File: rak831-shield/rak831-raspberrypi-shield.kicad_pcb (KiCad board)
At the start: 2 copper layers, 59.1 x 73.7 mm, 2 parts, among them P1 CONN_02X20, P2 CONN_02X12

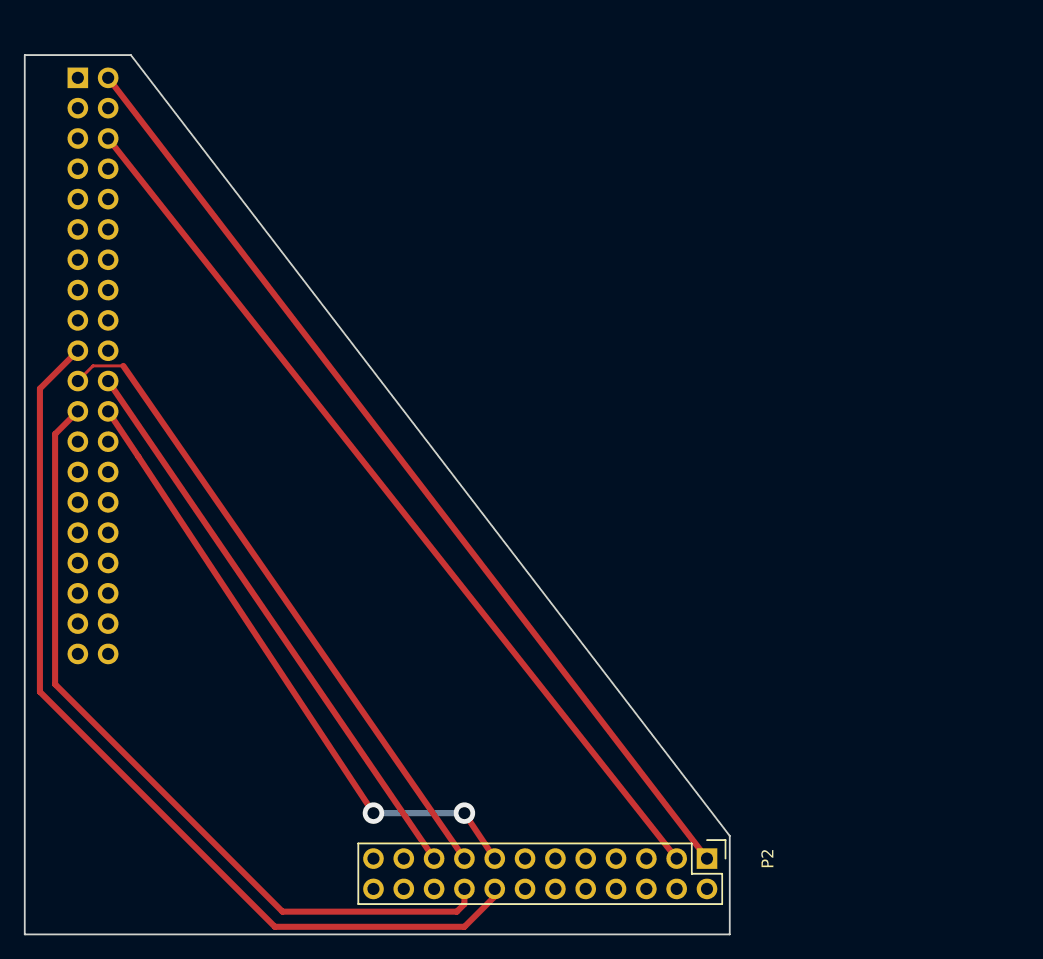
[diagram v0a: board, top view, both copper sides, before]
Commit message: Versión invertida y con pistas más gruesas.
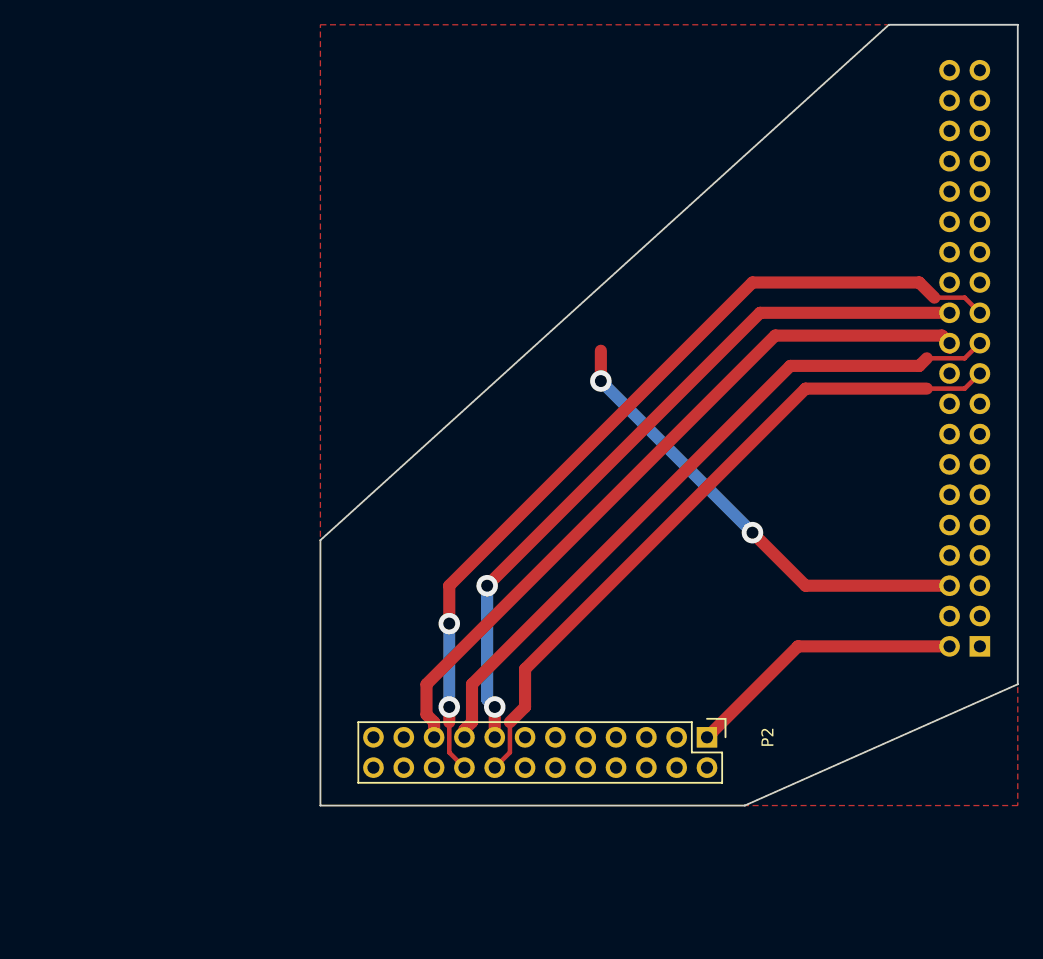
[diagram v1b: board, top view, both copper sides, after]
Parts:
- moved P1 89.3 mm to (134.6, 135.9), turned to 90 degrees
- moved P2 10.2 mm to (111.8, 143.5)
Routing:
- net Net-(P1-Pad2): track 82.4 -> 23.5 mm
- net Net-(P1-Pad6): track 76.9 -> 38.9 mm, vias 0 -> 2
- net Net-(P1-Pad19): track 77.8 -> 57.7 mm
- net Net-(P1-Pad22): track 48.4 -> 61.8 mm
- net Net-(P1-Pad24): track 52.5 -> 61.2 mm
- net Net-(P1-Pad21): track 54.5 -> 59.1 mm
- net Net-(P1-Pad23): track 67.4 -> 71.8 mm, vias 0 -> 2
- added copper zone on F.Cu, net Net-(P1-Pad6)
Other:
- board size 59.1 x 73.7 mm -> 58.4 x 65.4 mm

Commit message: Versión más compacta
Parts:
- moved P2 7.62 mm to (119.4, 143.5)
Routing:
- net Net-(P1-Pad6): track 38.9 -> 51.9 mm
- net Net-(P1-Pad23): track 71.8 -> 61.6 mm, vias 2 -> 0
- net Net-(P1-Pad24): track 61.2 -> 51.2 mm, vias 2 -> 0
- net Net-(P1-Pad19): track 57.7 -> 49.9 mm
- net Net-(P1-Pad2): track 23.5 -> 15.9 mm
- net Net-(P1-Pad22): track 61.8 -> 54.6 mm, vias 0 -> 2
- net Net-(P1-Pad21): track 59.1 -> 52.7 mm, vias 0 -> 2
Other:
- board size 58.4 x 65.4 mm -> 48.9 x 65.4 mm
